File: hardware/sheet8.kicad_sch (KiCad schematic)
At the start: 0 parts

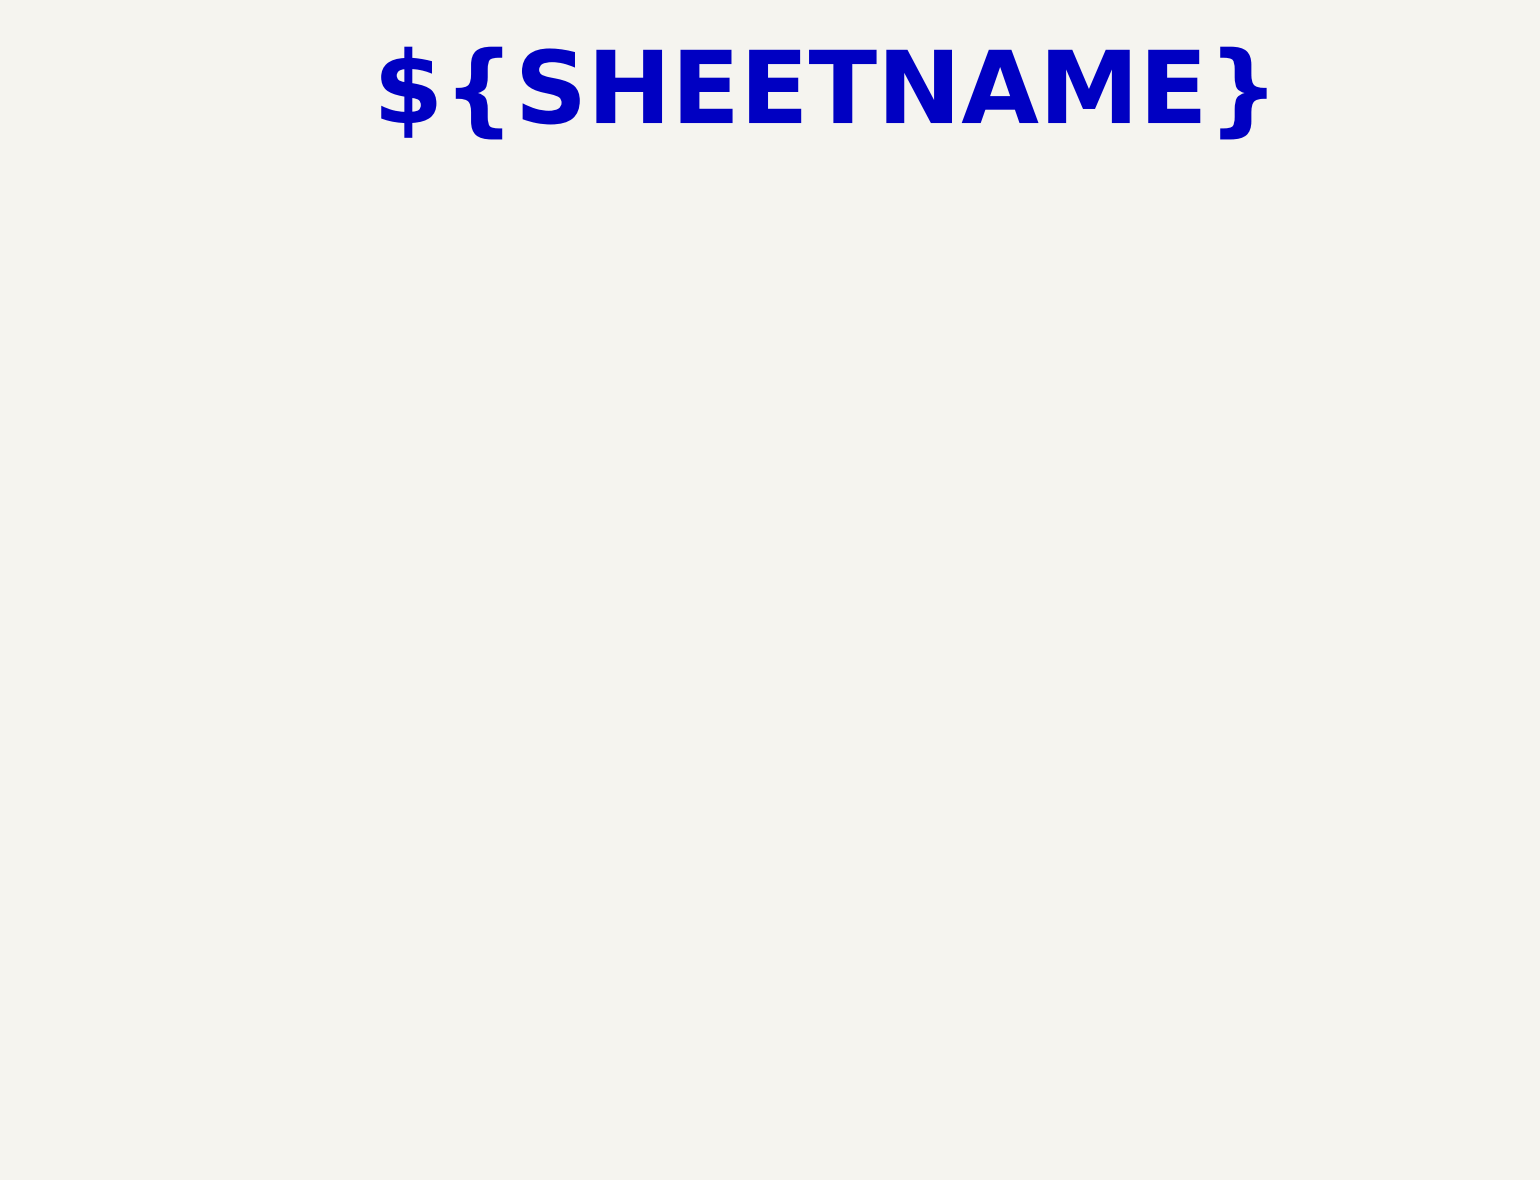
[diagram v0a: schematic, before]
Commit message: hardware(feat): add 16x2 lcd with pcf8574 on i2c1 (#5)
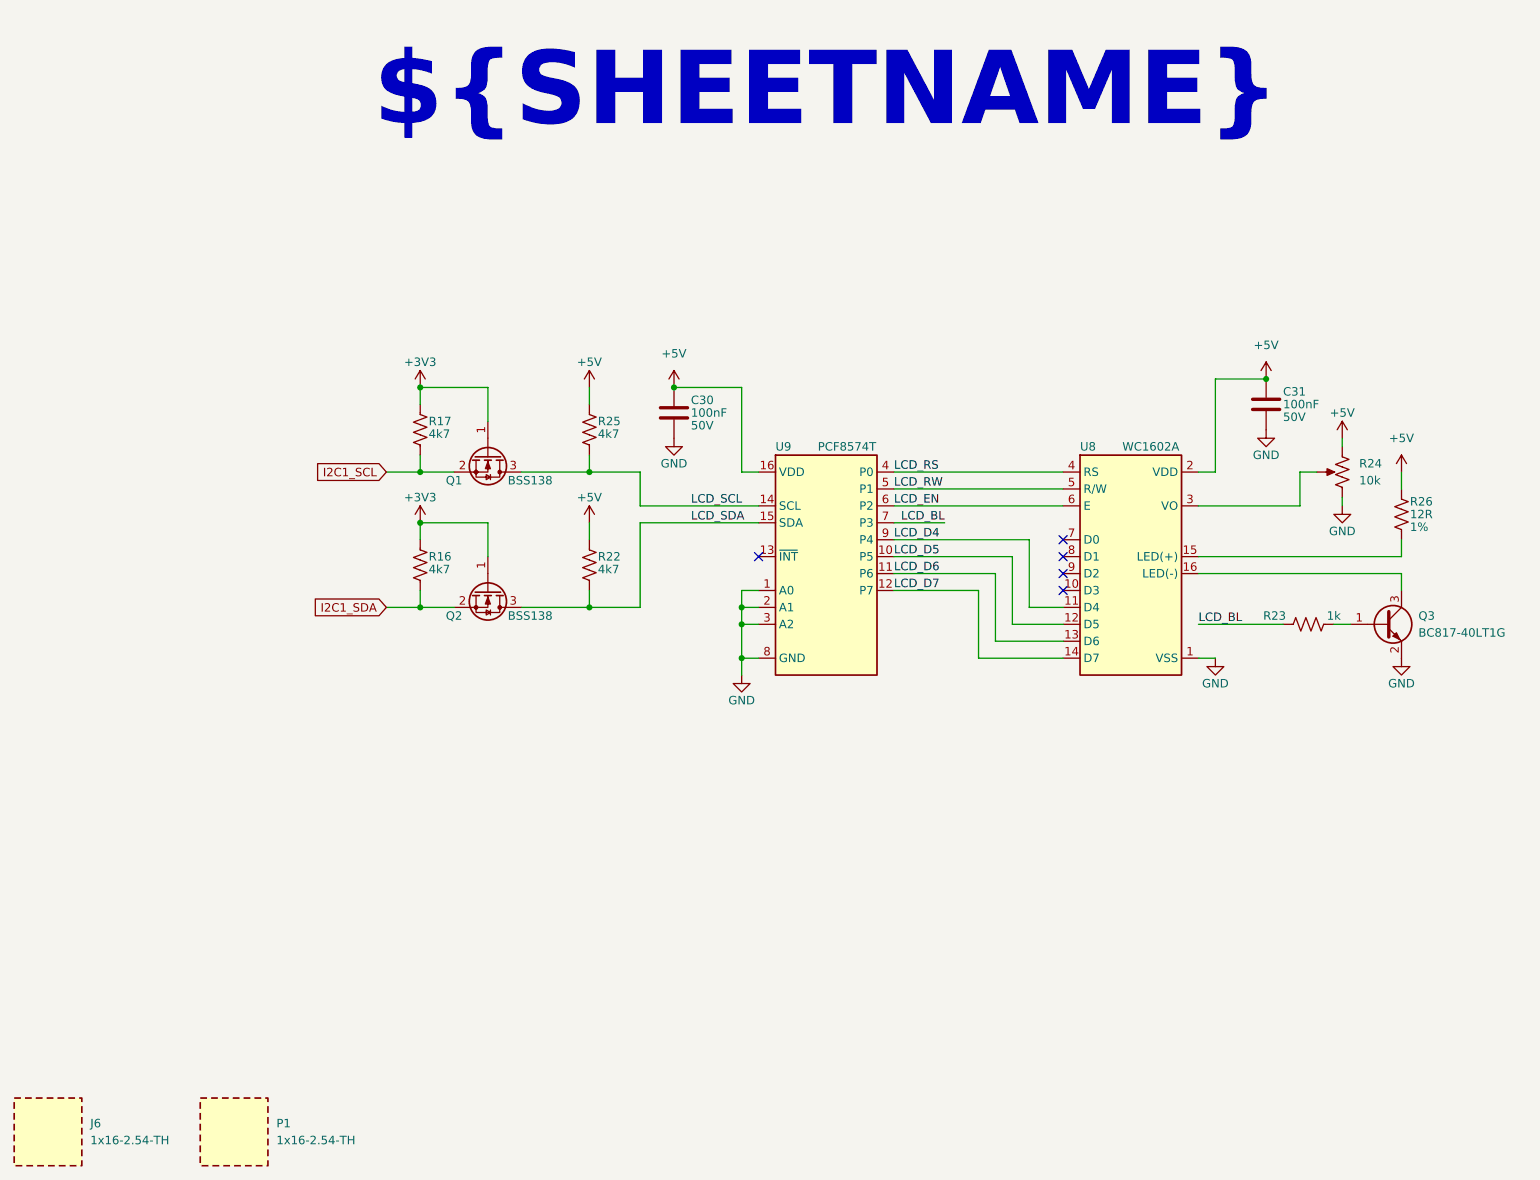
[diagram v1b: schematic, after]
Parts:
- added C30, C31: 100nF, 02_capacitors:C_0603_1608Metric, symbol 02_capacitors:CAP_100nF-50V-10%-X7R-0603
- added J6: 1x16-2.54-TH, symbol 08_connectors:CON-SKT_1x16-2.54-TH
- added P1: 1x16-2.54-TH, symbol 08_connectors:CON-HDR_1x16-2.54-TH
- added Q1, Q2: BSS138, 05_transistors:SOT-23, symbol 05_transistors:FET-N_50V-220mA-3.5R-SOT-23
- added Q3: BC817-40LT1G, 05_transistors:SOT-23, symbol 05_transistors:BJT-N_45V-500mA-SOT-23
- added R16, R17, R22, R25: 4k7, 01_resistors:R_0603_1608Metric, symbol 01_resistors:RES_4.7K-0.1W-1%-0603
- added R23: 1k, 01_resistors:R_0603_1608Metric, symbol 01_resistors:RES_1K-0.1W-1%-0603
- added R24: 10k, 01_resistors:TH_3362P, symbol 01_resistors:POT_10K-3362P-1-103LF-TH
- added R26: 12R, 01_resistors:R_0805_2012Metric, symbol 01_resistors:RES_12R-0.125W-1%-0805
- added U8: WC1602A, 11_modules:WC1602A, symbol 11_modules:MOD-DISP_WC1602A
- added U9: PCF8574T, 06_ics:SOIC-16W_7.5x10.3mm_P1.27mm, symbol 06_ics:IC-IF_PCF8574T
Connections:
- new net: Q3.1 (B), R23.2
- new net: Q3.3 (C), U8.16 (LED(-))
- new net: R26.2, U8.15 (LED(+))
- new net: R24.2, U8.3 (VO)
- new net +3V3: Q1.1 (G), Q2.1 (G), R16.1, R17.1
- new net +5V: C30.1, C31.1, R22.1, R24.3, R25.1, R26.1, U8.2 (VDD), U9.16 (VDD)
- new net GND: C30.2, C31.2, Q3.2 (E), R24.1, U8.1 (VSS), U9.1 (A0), U9.2 (A1), U9.3 (A2), U9.8 (GND)
- new net I2C1_SCL: Q1.2 (S), R17.2
- new net I2C1_SDA: Q2.2 (S), R16.2
- new net LCD_BL: R23.1, U9.7 (P3)
- new net LCD_D4: U8.11 (D4), U9.9 (P4)
- new net LCD_D5: U8.12 (D5), U9.10 (P5)
- new net LCD_D6: U8.13 (D6), U9.11 (P6)
- new net LCD_D7: U8.14 (D7), U9.12 (P7)
- new net LCD_EN: U8.6 (E), U9.6 (P2)
- new net LCD_RS: U8.4 (RS), U9.4 (P0)
- new net LCD_RW: U8.5 (R/W), U9.5 (P1)
- new net LCD_SCL: Q1.3 (D), R25.2, U9.14 (SCL)
- new net LCD_SDA: Q2.3 (D), R22.2, U9.15 (SDA)
- no-connect marks 0 -> 5
